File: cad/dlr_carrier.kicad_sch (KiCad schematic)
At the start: 0 parts

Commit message: 🗺 feat(cad): scripted schematic + board pipeline, 4-layer stack
The committed board had almost every pad on +3V3 — no 5V_RAIL, VBAT or SDA1 net
existed on it at all — so the gerbers in output/ were never a valid board. Cause:
"Update PCB from Schematic" is GUI-only, so nothing kept the board honest, and the
schematic generator itself was merging nets.

Schematic generator:
  * power stubs now run along the pin direction; they used to be forced up or down
    regardless, which drove a 5V_RAIL stub straight through the buck inductor's
    BUCK_SW pin
  * PWR_FLAGs are placed by rule — any net that reaches a power-input pin with no
    power-output pin gets exactly one — instead of a hardcoded list, which is what
    the new VBAT and CHG_VCC rails needed
  * placement is deterministic; it used Python's salted hash(), so no two runs
    produced the same schematic
  * sch_guard fails the build on any cross-net wire/pin collision
  * ~700 lines of dead single-sheet generator removed
  ERC: 0 violations across all 8 sheets.

Board pipeline (cad/drawing/, all scripted, no GUI step):
  sync_pcb      rebuilds every footprint from the library and reassigns every pad
                net from the SKiDL netlist — the replacement for F8
  board_setup   4-layer SIG/GND/5V/SIG stack, rules, net classes, planes (ADR-016)
  route_pcb     DSN -> Freerouting -> SES, after patching the DSN so plane layers
                are "power" (the router was slicing the planes with signals) and
                the plane declarations are dropped (the router had been leaving
                GND and 5V pads with no path to the plane at all)
  stitch_planes vias from surface pads into their plane
  close_gaps    closes what the router leaves, using real segment-to-segment
                clearance; it never forces copper through another net

DRC: 265 unconnected -> 5, with no clearance, short, annular-ring or courtyard
errors. The remaining 5 are escapes on the DF40, the VQFN and the MSOP; they are
l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
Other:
- removed sheet POWER
- added sheet POWER RAILS (dlr_carrier-power.kicad_sch)
- added sheet SOLAR MPPT CHARGER (dlr_carrier-charger.kicad_sch)
- sheet ANEMOMETER RS-485 ports: added ANEMO_DE; removed NC_CM4_31
- sheet CM4 SoM ports: added ANEMO_DE, CHG_STAT1, CHG_STAT2; removed NC_CM4_31

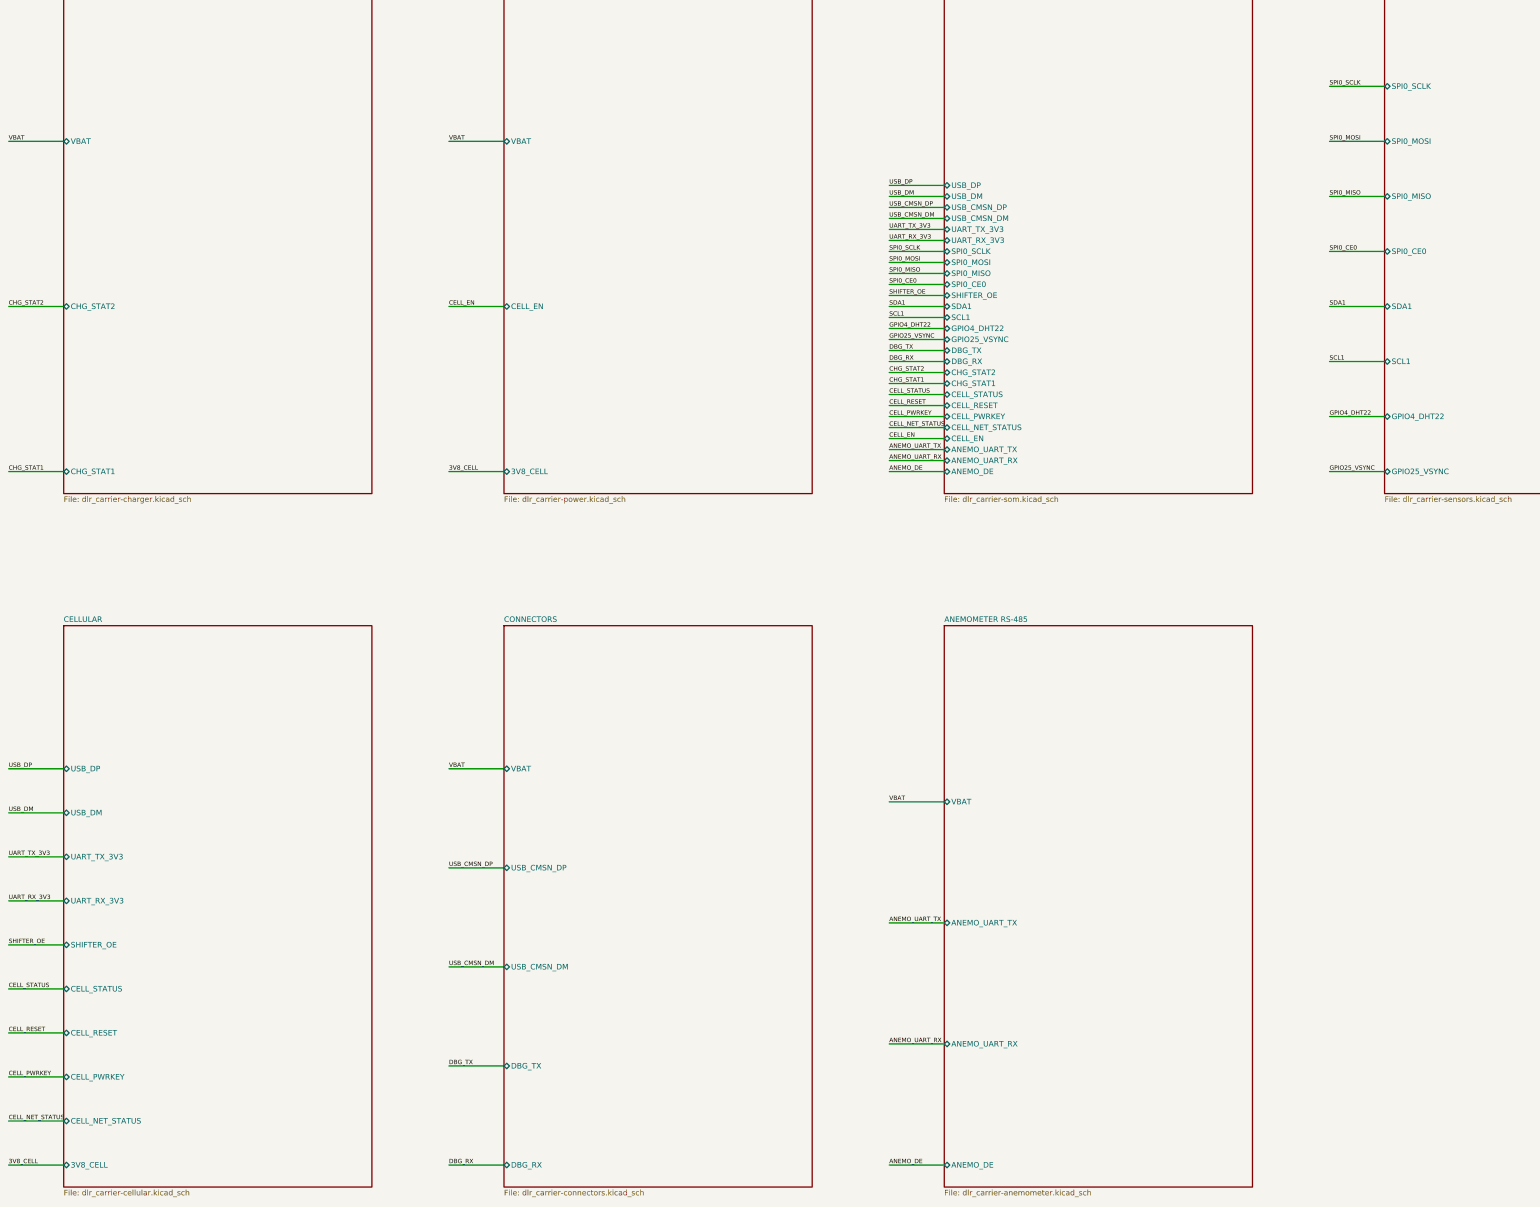
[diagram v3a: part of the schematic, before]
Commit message: 🩺 refactor(schematic): cross-sheet nets via global labels, no sheet pins
Three attempts at making the hierarchical sheet-pin mechanism pass KiCad 9 failed
(project name, instance paths, label type), so the mechanism goes. Cross-sheet nets
now connect by name through global labels on the child sheets; the root carries
sheet symbols only — no pins, no stub wires, no labels.

That removes the whole hier_label_mismatch / label_dangling class rather than
chasing it, and it matches the connectivity style the generate-schematic skill
already prescribes for this project ("all inter-block connections use net labels").

kicad-sch-api's add_global_label still does not serialize, so the labels are emitted
as hierarchical and rewritten in the saved sheet.

Co-Authored-By: Claude Opus 5 <noreply@anthropic.com>
Claude-Session: https://claude.ai/code/session_011xr7VCL7rkJj2WE2uQF7sF
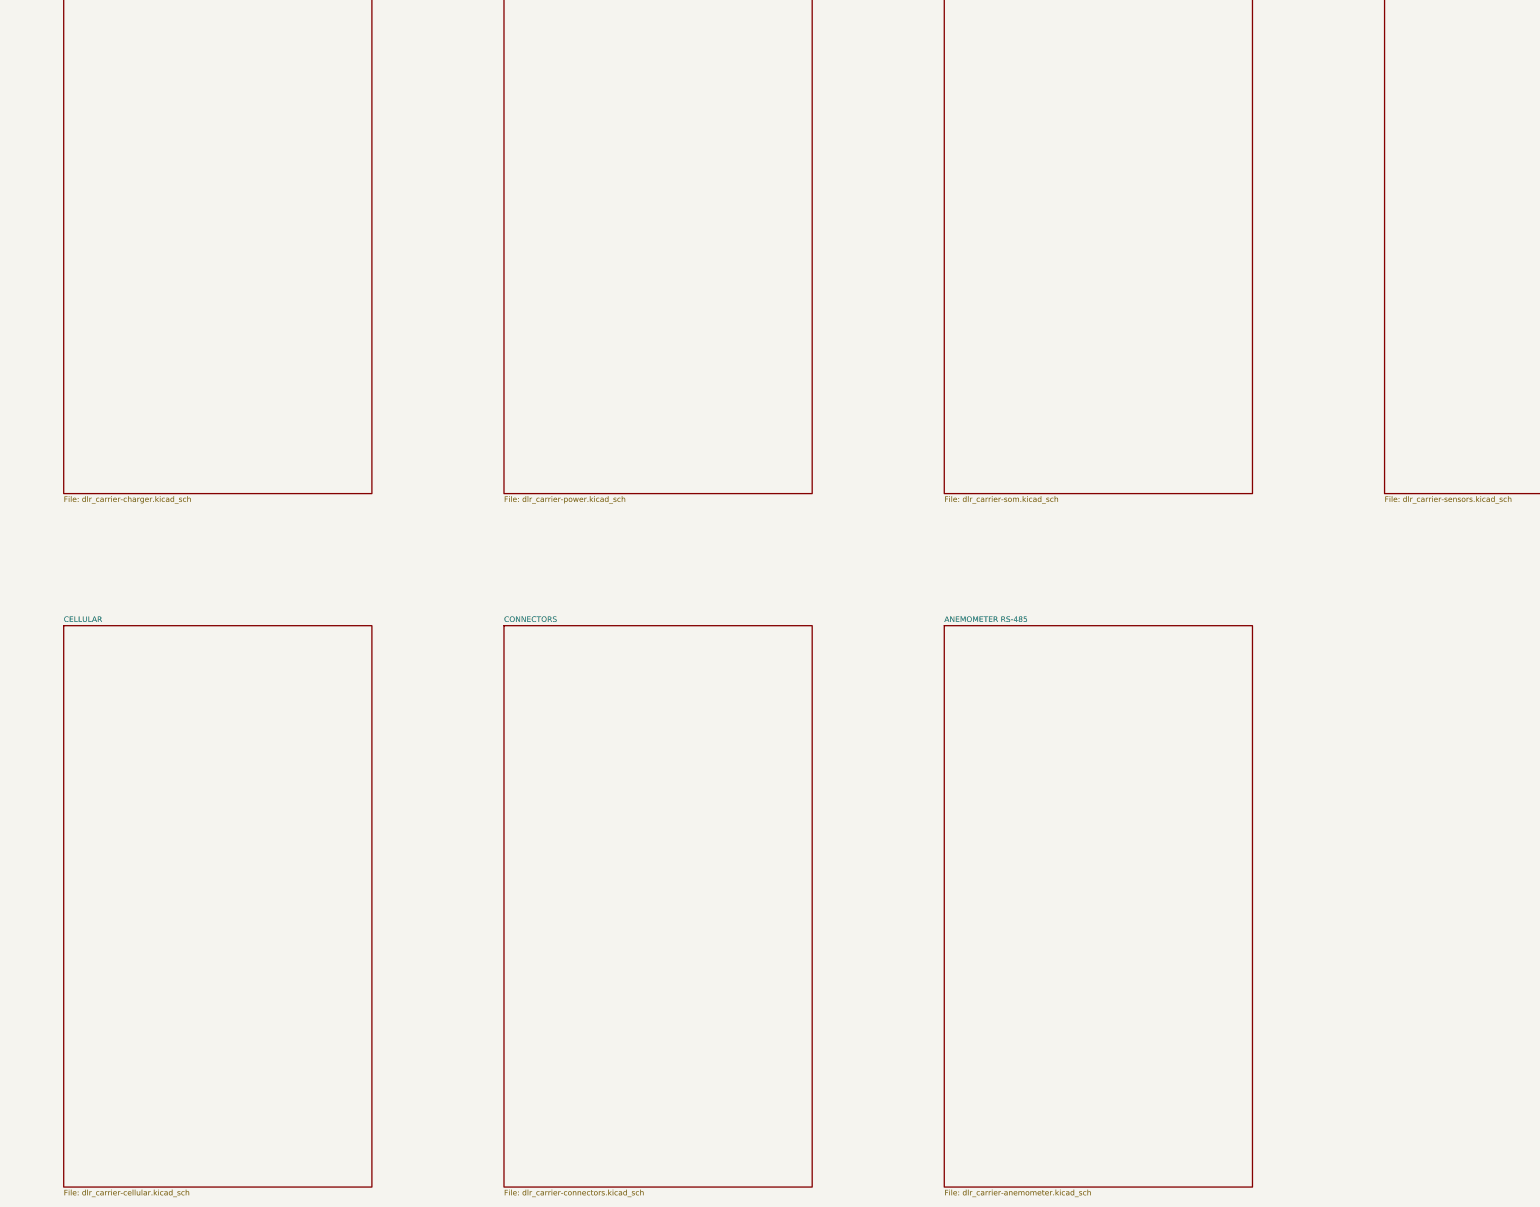
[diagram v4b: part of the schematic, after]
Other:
- sheet ANEMOMETER RS-485 ports: added none; removed ANEMO_DE, ANEMO_UART_RX, ANEMO_UART_TX, VBAT
- sheet CELLULAR ports: added none; removed 3V8_CELL, CELL_NET_STATUS, CELL_PWRKEY, CELL_RESET, CELL_STATUS, SHIFTER_OE, UART_RX_3V3, UART_TX_3V3, USB_DM, USB_DP
- sheet CM4 SoM ports: added none; removed ANEMO_DE, ANEMO_UART_RX, ANEMO_UART_TX, CELL_EN, CELL_NET_STATUS, CELL_PWRKEY, CELL_RESET, CELL_STATUS, CHG_STAT1, CHG_STAT2, DBG_RX, DBG_TX, GPIO25_VSYNC, GPIO4_DHT22, SCL1, SDA1, SHIFTER_OE, SPI0_CE0, SPI0_MISO, SPI0_MOSI, SPI0_SCLK, UART_RX_3V3, UART_TX_3V3, USB_CMSN_DM, USB_CMSN_DP, USB_DM, USB_DP
- sheet CONNECTORS ports: added none; removed DBG_RX, DBG_TX, USB_CMSN_DM, USB_CMSN_DP, VBAT
- sheet IEEE 738 SENSORS ports: added none; removed GPIO25_VSYNC, GPIO4_DHT22, SCL1, SDA1, SPI0_CE0, SPI0_MISO, SPI0_MOSI, SPI0_SCLK
- sheet POWER RAILS ports: added none; removed 3V8_CELL, CELL_EN, VBAT
- sheet SOLAR MPPT CHARGER ports: added none; removed CHG_STAT1, CHG_STAT2, VBAT
